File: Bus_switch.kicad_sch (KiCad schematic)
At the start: 15 parts, among them J3 Conn_01x04_Pin, U1 SN74CB3Q3245PWR

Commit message: inital layout
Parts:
- removed R11, R2, R3, R5, R7, R8, R9: 10kΩ, PCM_JLCPCB:R_0402, symbol PCM_JLCPCB-Resistors:0402,10kΩ

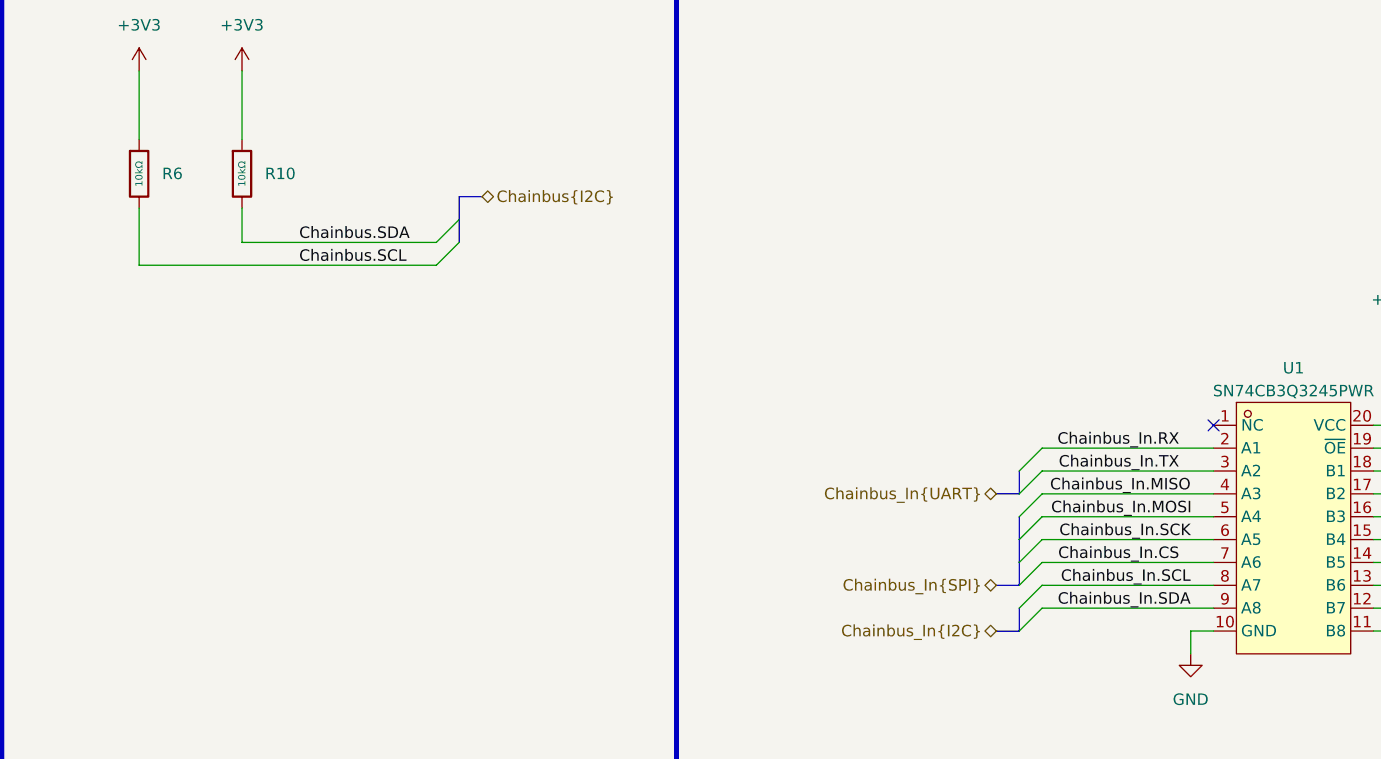
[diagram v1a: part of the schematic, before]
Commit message: commit before removing all the diodes :"
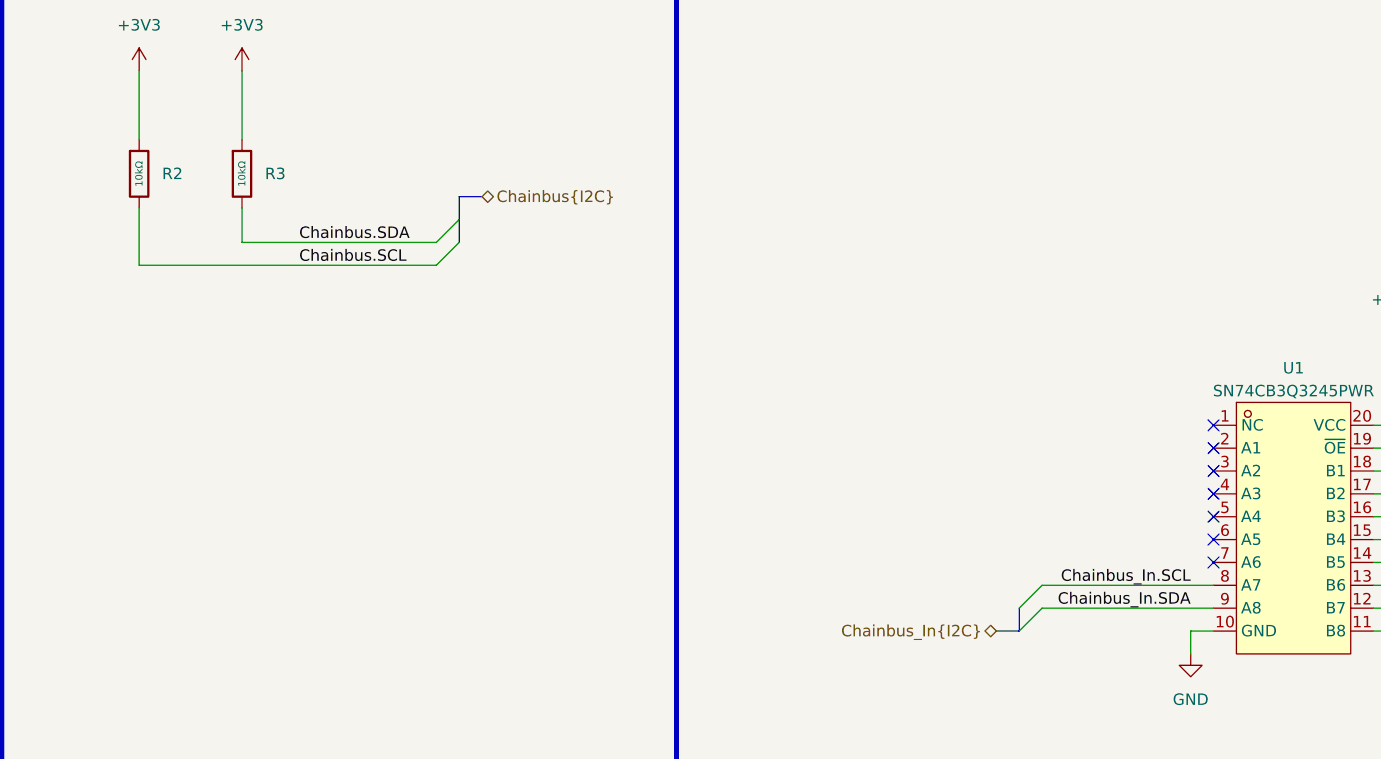
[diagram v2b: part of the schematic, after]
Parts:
- removed R10, R6: 10kΩ, PCM_JLCPCB:R_0402, symbol PCM_JLCPCB-Resistors:0402,10kΩ
- added R2, R3: 10kΩ, PCM_JLCPCB:R_0603, symbol PCM_JLCPCB-Resistors:0603,10kΩ
- J3: KiLib_Generator (none) -> connector/pin_header_socket
- R1: Field4 (none) -> 0402WGF3300TCE
- R19: Field4 (none) -> ${REFERENCE}
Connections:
- net +3V3: now also R2.1, R3.1
- net Chainbus.SCL: now also R2.2
- net Chainbus.SDA: now also R3.2
- net Chainbus_In.CS: no longer names the net of U1.7 (A6)
- net Chainbus_In.MISO: no longer names the net of U1.4 (A3)
- net Chainbus_In.MOSI: no longer names the net of U1.5 (A4)
- net Chainbus_In.RX: no longer names the net of U1.2 (A1)
- net Chainbus_In.SCK: no longer names the net of U1.6 (A5)
- net Chainbus_In.TX: no longer names the net of U1.3 (A2)
- no-connect marks 1 -> 7
